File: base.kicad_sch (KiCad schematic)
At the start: 7 parts, among them J1 Raspberry_Pi_2_3, M5 Stepper_Motor_bipolar, M6 Stepper_Motor_bipolar, M7 Stepper_Motor_bipolar, M8 Stepper_Motor_bipolar

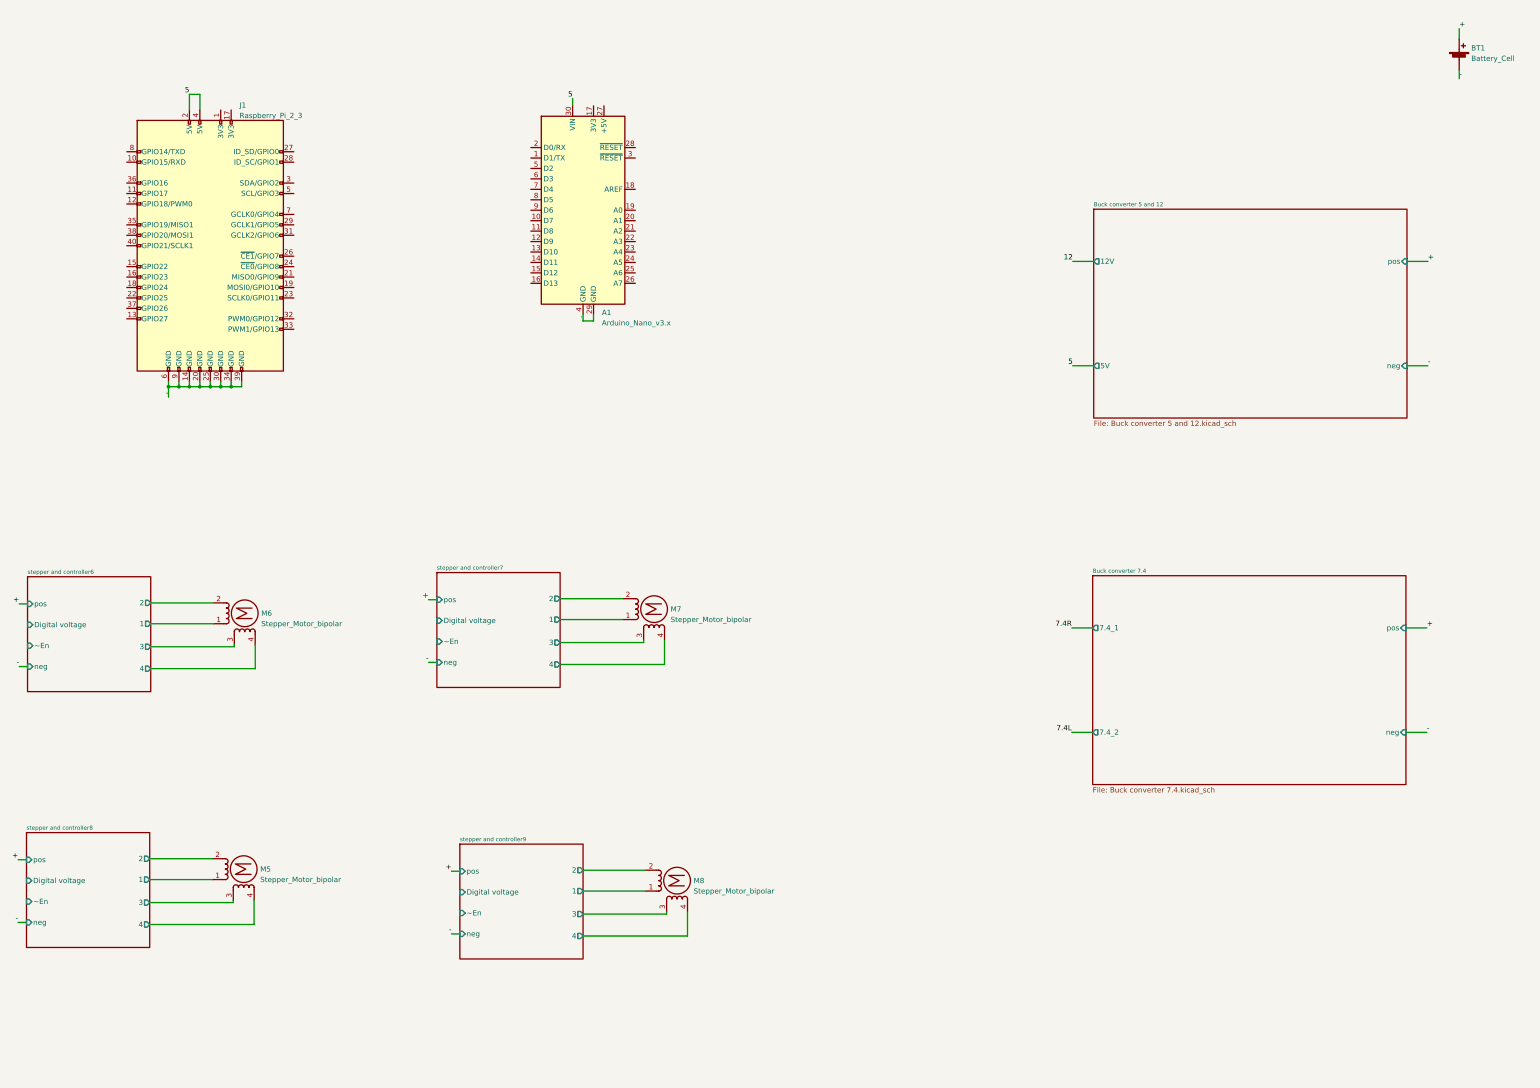
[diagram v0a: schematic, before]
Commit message: base schematic and PCB made
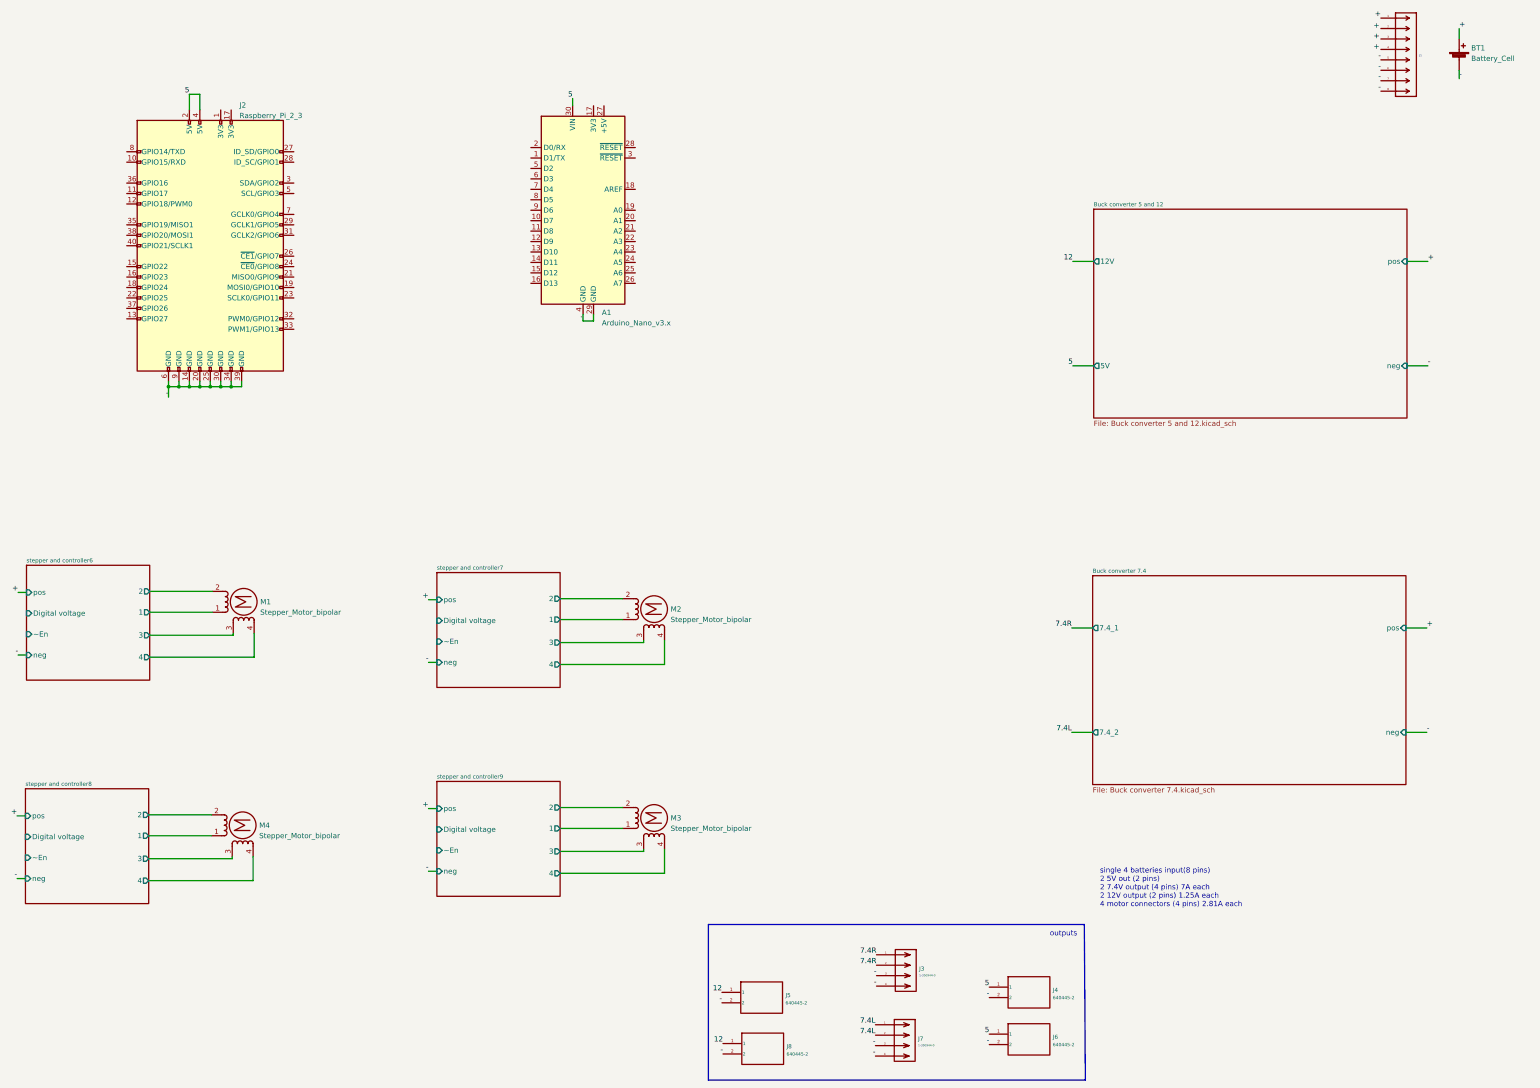
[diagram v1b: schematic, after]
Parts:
- added J1: 282856-8, Connectors:282856-8, symbol Connectors:282856-8
- added J3, J7: 1-350944-0, Connectors:1-350944-0, symbol Connectors:1-350944-0
- added J4, J5, J6, J8: 640445-2, Connectors:640445-2, symbol Connectors:640445-2
- BT1: footprint (none) -> my_footprints:282856-8; now left out of the parts list
- J2: renamed from J1; footprint (none) -> Modules:Raspberry pi 4
- M1: renamed from M6; footprint (none) -> Connectors:1-350944-0
- M2: renamed from M7; footprint (none) -> Connectors:1-350944-0
- M3: renamed from M8; footprint (none) -> Connectors:1-350944-0
- M4: renamed from M5; footprint (none) -> Connectors:1-350944-0
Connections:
- net +: now also J1.1, J1.2, J1.3, J1.4
- net -: now also J1.5, J1.6, J1.7, J1.8, J3.3, J3.4, J4.2, J5.2, J6.2, J7.3, J7.4, J8.2
- net 12: now also J5.1, J8.1
- net 5: now also J4.1, J6.1
- net 7.4L: now also J7.1, J7.2
- net 7.4R: now also J3.1, J3.2
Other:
- note added: "outputs"
- note added: "single 4 batteries input(8 pins) 2 5V out (2 pins) 2 7.4V output (4 pins) 7A each 2 12V output (2 pins) 1.25A each 4 motor connectors (4 pins) 2.81A each"
- moved on the sheet: M1, M3, M4
